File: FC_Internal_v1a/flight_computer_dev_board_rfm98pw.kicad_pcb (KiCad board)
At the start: 4 copper layers, 88 x 94.5 mm, 102 parts, among them IC1 RP2040_QFN56, IC2 AZ1117CH-3.3TRG1, J1 Conn_ARM_JTAG_SWD_10, J10 BM04B-SRSS-TB(LF)(SN), J11 BM04B-SRSS-TB(LF)(SN), J12 BM04B-SRSS-TB(LF)(SN), J13 Breakout, J14 Battery, J15 Breakout, J2 FC to EPS Connector, J3 Life Makes Lemonade, J4 104031-0811, J5 BM04B-SRSS-TB(LF)(SN), J6 Conn_Coaxial, J7 Breakout, J8 USB_B_Micro, J9 BM04B-SRSS-TB(LF)(SN), SW1 KMR2, SW2 KMR2, U10 AP3602AKTR-G1, U3 MAX706RESA, U4 RFM98PW, U5 RFM9xBreakout, U6 W25Q128JV, U7 LSM6DSOTR, U8 LSM303AGRTR, U9 MCP25625-E/ML, Y1 12MHZ, Y3 16MHZ 12 pf

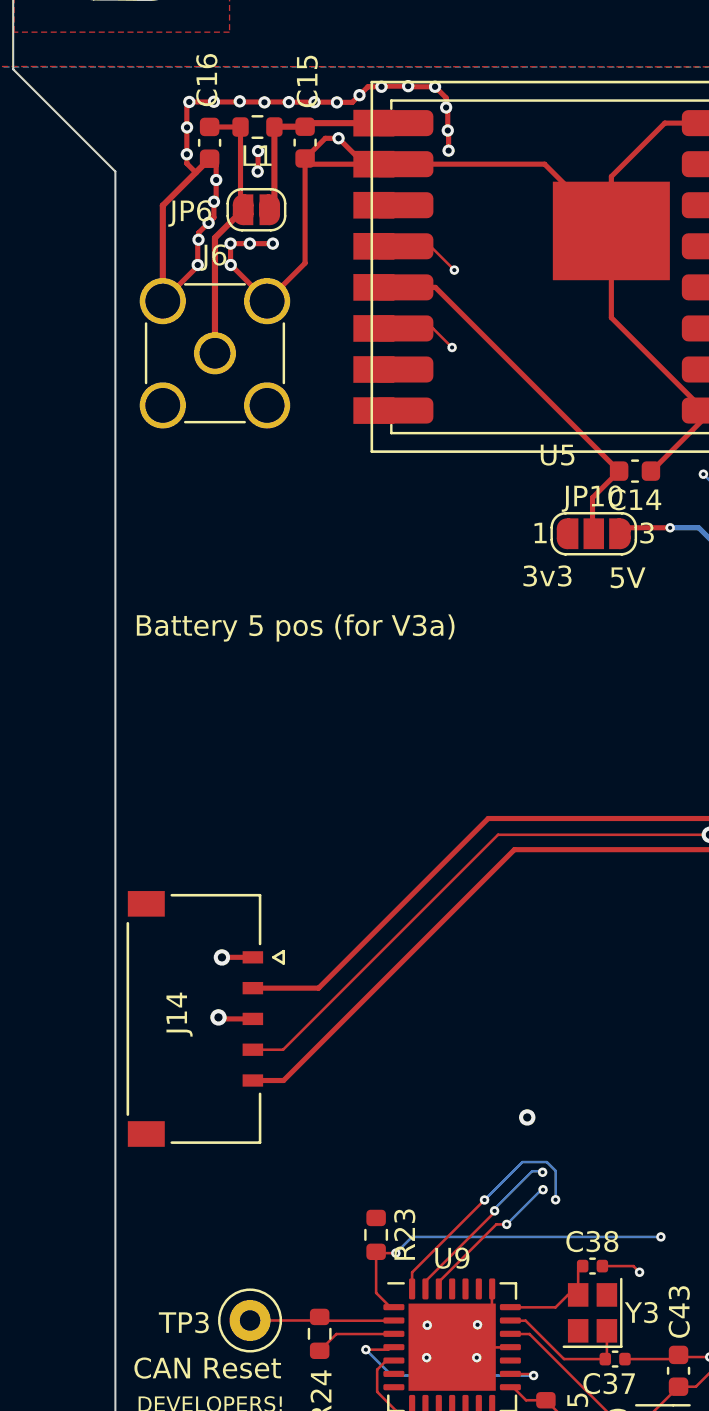
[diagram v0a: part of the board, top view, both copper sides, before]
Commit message: Fixed Impedance Matching
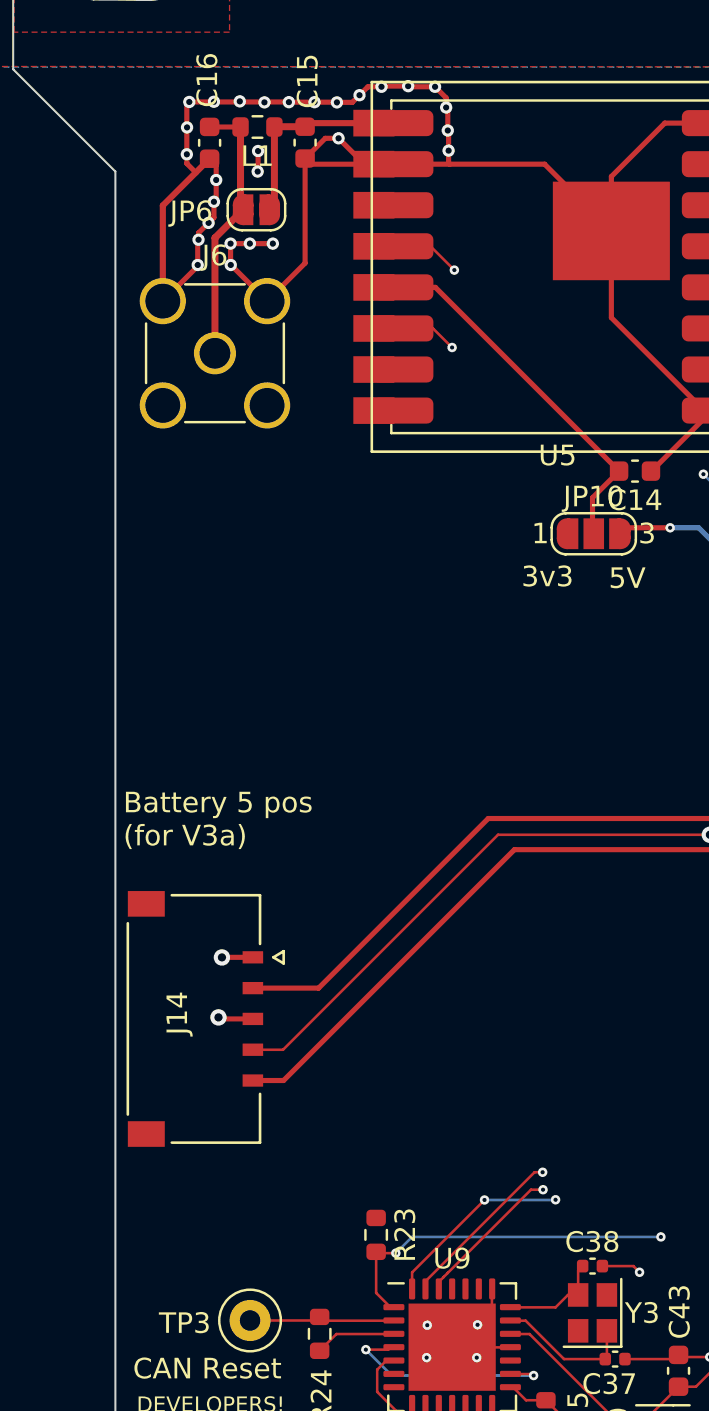
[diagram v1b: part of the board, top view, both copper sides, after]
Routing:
- net SPI0_MISO: track 137.2 -> 134.9 mm
- net GND: track 248.5 -> 249.1 mm, vias 74 -> 73
- net SPI0_MOSI: track 138.6 -> 138.5 mm, vias 9 -> 8
- net SPI0_SCK: track 139.8 -> 139.9 mm, vias 9 -> 8

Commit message: Major Schematic Refactor
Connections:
- net 3v3 Spec renamed /3v3 Spec
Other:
- board text added: "Made with the help of LMAO and LMBFAO"
- board text removed: "Made with the help of LMAO and LMBAO"
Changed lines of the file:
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@@
   (net 5 "3.3V")
   (net 6 "VBUS")
-  (net 7 "3v3 Spec")
+  (net 7 "/3v3 Spec")
   (net 8 "VCC_RF1")
   (net 9 "RF1_ANT")
@@
       (stroke (width 0.1) (type solid)) (layer "F.Fab"))
     (pad "1" smd roundrect (at -0.775 0 90) (size 0.9 0.95) (layers "F.Cu" "F.Paste" "F.Mask") (roundrect_rratio 0.25)
-      (net 7 "3v3 Spec") (pinfunction "1") (pintype "passive"))
+      (net 7 "/3v3 Spec") (pinfunction "1") (pintype "passive"))
     (pad "2" smd roundrect (at 0.775 0 90) (size 0.9 0.95) (layers "F.Cu" "F.Paste" "F.Mask") (roundrect_rratio 0.25)
       (net 4 "GND") (pinfunction "2") (pintype "passive"))
@@
       (net 4 "GND") (pinfunction "ADJ/GND") (pintype "passive"))
     (pad "2" smd rect (at -3.15 0 180) (size 2 1.5) (layers "F.Cu" "F.Paste" "F.Mask")
-      (net 7 "3v3 Spec") (pinfunction "OUTPUT") (pintype "passive"))
+      (net 7 "/3v3 Spec") (pinfunction "OUTPUT") (pintype "passive"))
     (pad "3" smd rect (at -3.15 2.3 180) (size 2 1.5) (layers "F.Cu" "F.Paste" "F.Mask")
       (net 6 "VBUS") (pinfunction "INPUT") (pintype "passive"))
     (pad "4" smd rect (at 3.15 0 180) (size 2 3.8) (layers "F.Cu" "F.Paste" "F.Mask")
-      (net 7 "3v3 Spec") (pinfunction "VOUT") (pintype "passive"))
+      (net 7 "/3v3 Spec") (pinfunction "VOUT") (pintype "passive"))
     (model "${KICAD6_3DMODEL_DIR}/Package_TO_SOT_SMD.3dshapes/SOT-223.wrl"
       (offset (xyz 0 0 0))
@@
       ))
     (pad "2" smd custom (at 0.65 0) (size 1 0.5) (layers "F.Cu" "F.Mask")
-      (net 7 "3v3 Spec") (pinfunction "B") (pintype "passive") (zone_connect 2) (thermal_bridge_angle 45)
+      (net 7 "/3v3 Spec") (pinfunction "B") (pintype "passive") (zone_connect 2) (thermal_bridge_angle 45)
       (options (clearance outline) (anchor rect))
       (primitives
@@
     (effects (font (size 1 1) (thickness 0.15)) (justify left bottom))
   )
-  (gr_text "Made with the help of LMAO and LMBAO" (at 175.44 140.58) (layer "F.SilkS")
+  (gr_text "Made with the help of LMAO and LMBFAO" (at 175.44 140.58) (layer "F.SilkS")
     (effects (font (size 1 1) (thickness 0.15)) (justify left bottom))
   )

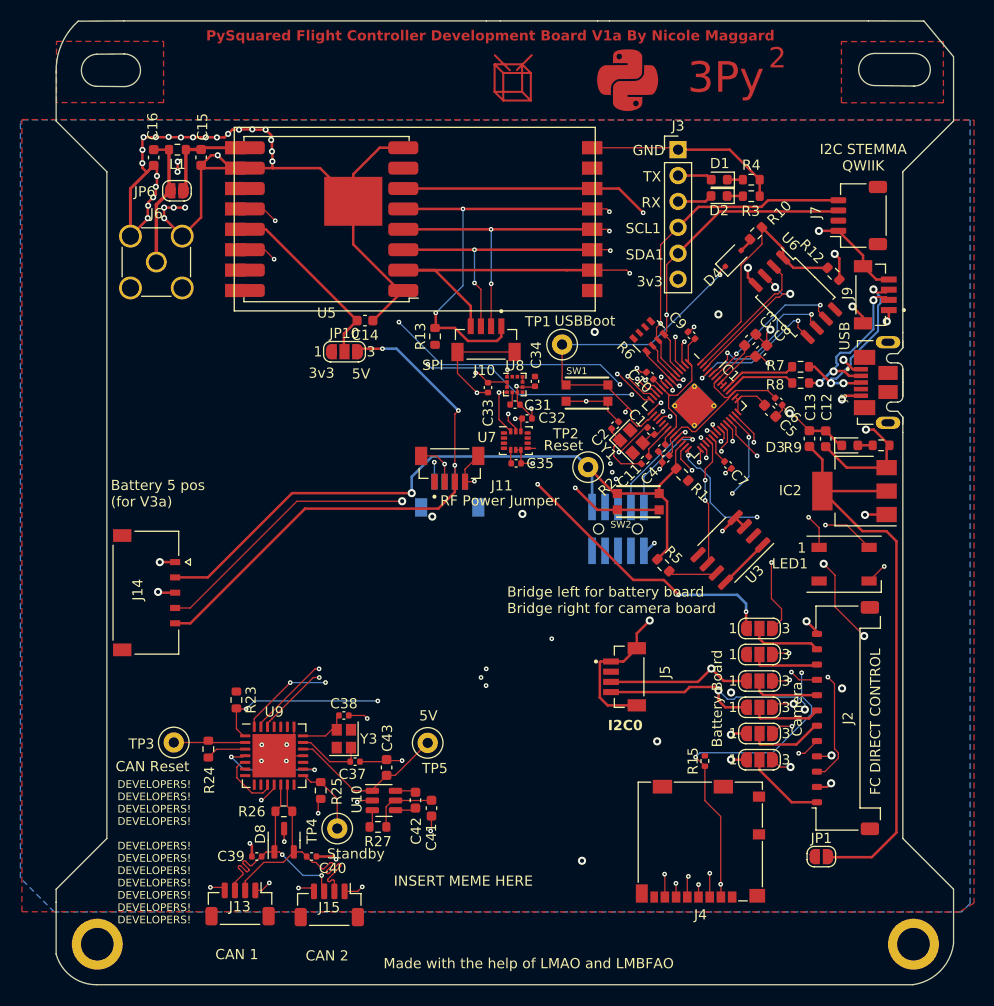
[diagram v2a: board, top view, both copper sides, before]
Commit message: Silkscreen Updates
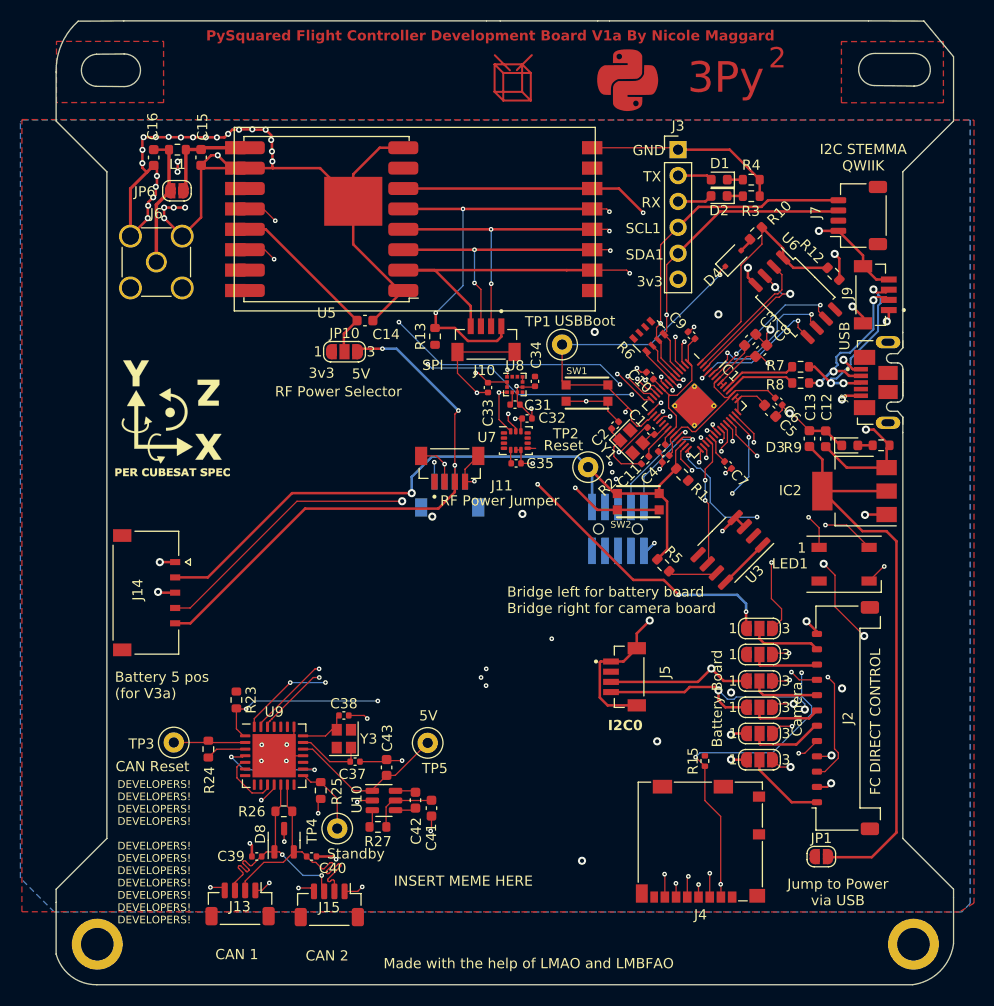
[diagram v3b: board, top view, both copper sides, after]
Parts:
- added REF**: Val**, mainboard:XYZ_cubesat-top, F.Cu at (154.7, 87.3)
- J3: value Life Makes Lemonade -> DNI
- moved G*** 5.00 mm to (193.1, 124.1)
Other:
- board text added: "A Total Solar Eclipse"
- board text added: "Jump to Power via USB"
- board text added: "RF Power Selector"
- board text removed: "M1 The Crab Nebula"
